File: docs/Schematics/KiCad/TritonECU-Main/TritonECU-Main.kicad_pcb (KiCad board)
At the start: 4 copper layers, 158 x 174 mm, 195 parts, among them J1 EEC-V 104, J301 VR spare, Q101 ISL9V3040S3ST, Q102 ISL9V3040S3ST, Q103 ISL9V3040S3ST, Q104 ISL9V3040S3ST, Q105 ISL9V3040S3ST, Q106 ISL9V3040S3ST, Q107 ISL9V3040S3ST, Q108 ISL9V3040S3ST, Q109 BSS138, Q201 ZXMS6005DGQTA, Q202 ZXMS6005DGQTA, Q203 ZXMS6005DGQTA, Q204 ZXMS6005DGQTA, Q205 ZXMS6005DGQTA, Q206 ZXMS6005DGQTA, Q207 ZXMS6005DGQTA, Q208 ZXMS6005DGQTA, Q401 NCV8405ASTT1G, Q402 NCV8405ASTT1G, Q403 NCV8405ASTT1G, Q404 NCV8405ASTT1G, Q405 NCV8405ASTT1G, Q406 NCV8405ASTT1G, Q407 NCV8405ASTT1G, Q408 NCV8405ASTT1G, Q501 NCV8405ASTT1G, Q502 NCV8405ASTT1G, Q503 NCV8405ASTT1G, Q504 NCV8408BDTRKG, Q505 NCV8405ASTT1G, Q506 NCV8405ASTT1G, Q507 NCV8405ASTT1G, U101 74HCT541, U102 TPS3823A-33DBVR, U301 MAX9926UAEE+T, U302 MAX9926UAEE+T, U303 MAX9926UAEE+T, U401 74HCT541, U402 74HC4051, U501 74HCT541, U601 TBD62083AFNG

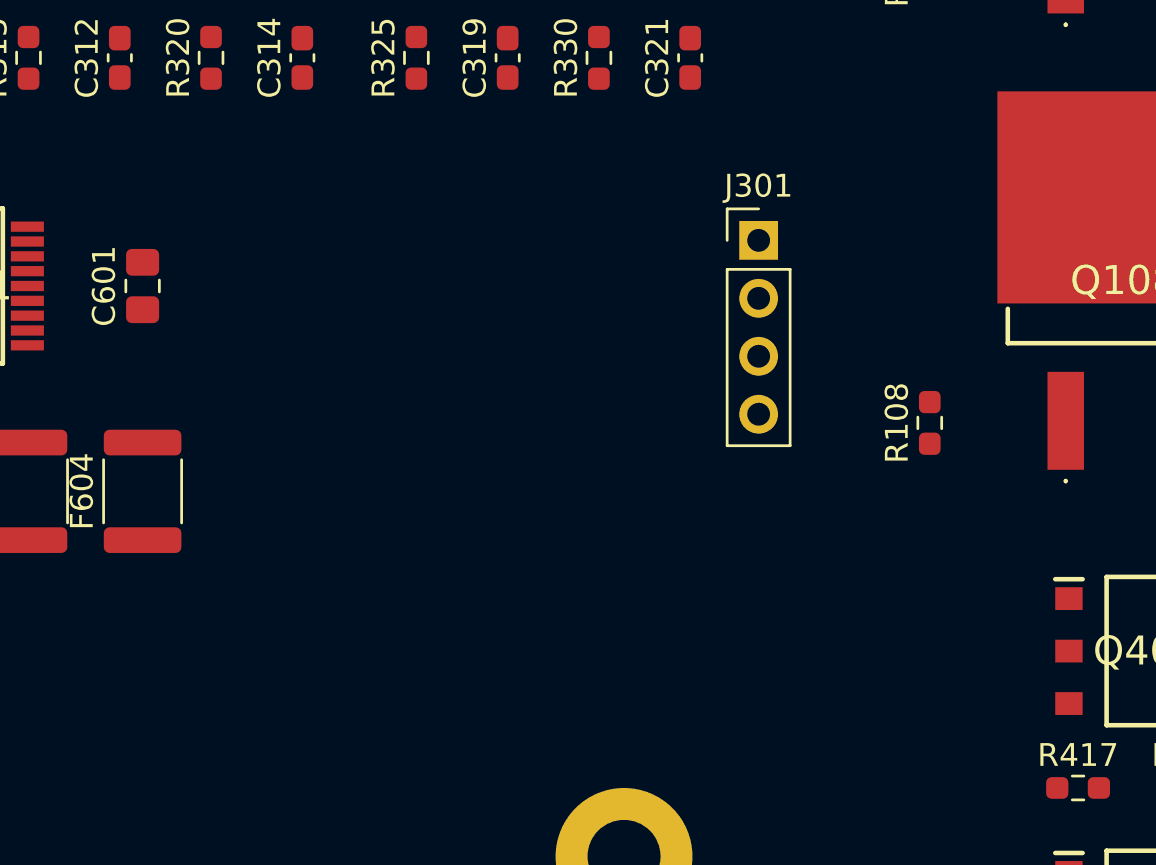
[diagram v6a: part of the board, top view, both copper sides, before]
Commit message: Carrier: VREF sheet, and the power board's +VIN is VPROT, not VPWR
VREF: NCV8772C 5.00 V on the protected rail, EN from the MCU; TPS2H160B-Q1
at 248 mA per feed, latch mode; LM74700-Q1 + DMN6040 ideal diode and
SMAJ24CA per feed; 100k/12.4k short-to-battery sense. Channel 2 drawn,
not fitted (one VREF pin, 90).

Fix: power board J3 +VIN is the LTC4364 OUTPUT (IC1 pin 1, after R2).
The carrier had it on VPWR, joining the surge stopper's output to its
raw input. It is now its own net, VPROT, which also feeds VREF.

gen_carrier_pcb.py: no-connect pins get their unconnected net (parity),
and --replace-sheet NAME re-places one sheet's parts.

Co-Authored-By: Claude Opus 5.5 <noreply@anthropic.com>
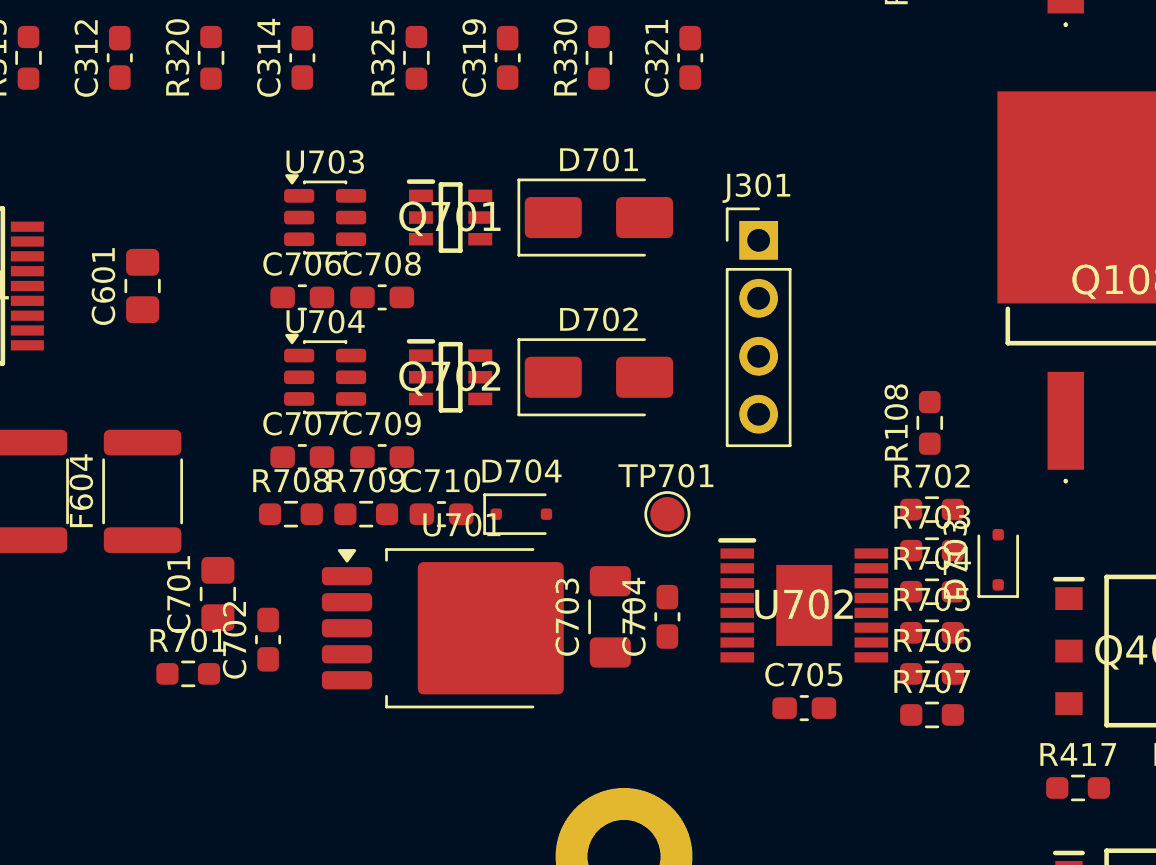
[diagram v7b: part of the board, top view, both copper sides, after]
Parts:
- added C701: 1u, Capacitor_SMD:C_0805_2012Metric_Pad1.18x1.45mm_HandSolder, F.Cu at (136.3, 113.5)
- added C702: 100n, Capacitor_SMD:C_0603_1608Metric_Pad1.08x0.95mm_HandSolder, F.Cu at (138.5, 115.5)
- added C703: 22u, Capacitor_SMD:C_1206_3216Metric_Pad1.33x1.80mm_HandSolder, F.Cu at (153.5, 114.5)
- added C704: 100n, Capacitor_SMD:C_0603_1608Metric_Pad1.08x0.95mm_HandSolder, F.Cu at (156.0, 114.5)
- added C705: 100n, Capacitor_SMD:C_0603_1608Metric_Pad1.08x0.95mm_HandSolder, F.Cu at (162.0, 118.5)
- added C706: 100n, Capacitor_SMD:C_0603_1608Metric_Pad1.08x0.95mm_HandSolder, F.Cu at (140.0, 100.5)
- added C707: 100n, Capacitor_SMD:C_0603_1608Metric_Pad1.08x0.95mm_HandSolder, F.Cu at (140.0, 107.5)
- added C708: 22n, Capacitor_SMD:C_0603_1608Metric_Pad1.08x0.95mm_HandSolder, F.Cu at (143.5, 100.5)
- added C709: 22n, Capacitor_SMD:C_0603_1608Metric_Pad1.08x0.95mm_HandSolder, F.Cu at (143.5, 107.5)
- added C710: 10n, Capacitor_SMD:C_0603_1608Metric_Pad1.08x0.95mm_HandSolder, F.Cu at (146.1, 110.0)
- added D701: SMAJ24CA, Diode_SMD:D_SMA, F.Cu at (153.0, 97.0)
- added D702: SMAJ24CA, Diode_SMD:D_SMA, F.Cu at (153.0, 104.0)
- added D703: BAT54J, Diode_SMD:D_SOD-323F, F.Cu at (170.5, 112.0)
- added D704: BAT54J, Diode_SMD:D_SOD-323F, F.Cu at (149.6, 110.0)
- added Q701: DMN6040SVTQ-7, Samacsys:SOT95P280X100-6N, F.Cu at (146.5, 97.0)
- added Q702: DMN6040SVTQ-7, Samacsys:SOT95P280X100-6N, F.Cu at (146.5, 104.0)
- added R701: 100k, Resistor_SMD:R_0603_1608Metric_Pad0.98x0.95mm_HandSolder, F.Cu at (135.0, 117.0)
- added R702: 10k, Resistor_SMD:R_0603_1608Metric_Pad0.98x0.95mm_HandSolder, F.Cu at (167.6, 109.8)
- added R703: 10k, Resistor_SMD:R_0603_1608Metric_Pad0.98x0.95mm_HandSolder, F.Cu at (167.6, 111.6)
- added R704: 10k, Resistor_SMD:R_0603_1608Metric_Pad0.98x0.95mm_HandSolder, F.Cu at (167.6, 113.4)
- added R705: 2.2k, Resistor_SMD:R_0603_1608Metric_Pad0.98x0.95mm_HandSolder, F.Cu at (167.6, 115.2)
- added R706: 4.7k, Resistor_SMD:R_0603_1608Metric_Pad0.98x0.95mm_HandSolder, F.Cu at (167.6, 117.0)
- added R707: 8.06k, Resistor_SMD:R_0603_1608Metric_Pad0.98x0.95mm_HandSolder, F.Cu at (167.6, 118.8)
- added R708: 100k, Resistor_SMD:R_0603_1608Metric_Pad0.98x0.95mm_HandSolder, F.Cu at (139.5, 110.0)
- added R709: 12.4k, Resistor_SMD:R_0603_1608Metric_Pad0.98x0.95mm_HandSolder, F.Cu at (142.8, 110.0)
- added TP701: VREF2, TestPoint:TestPoint_Pad_D1.5mm, F.Cu at (156.0, 110.0)
- added U701: NCV8772CDT504RKG, Package_TO_SOT_SMD:TO-252-5_TabPin3, F.Cu at (147.0, 115.0)
- added U702: TPS2H160BQPWPRQ1, Samacsys:SOP65P640X120-17N, F.Cu at (162.0, 114.0)
- added U703: LM74700QDBVRQ1, Package_TO_SOT_SMD:SOT-23-6, F.Cu at (141.0, 97.0)
- added U704: LM74700QDBVRQ1, Package_TO_SOT_SMD:SOT-23-6, F.Cu at (141.0, 104.0)
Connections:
- DB1 pad B3: VPWR -> VPROT
- DB1 pad B4: VPWR -> VPROT

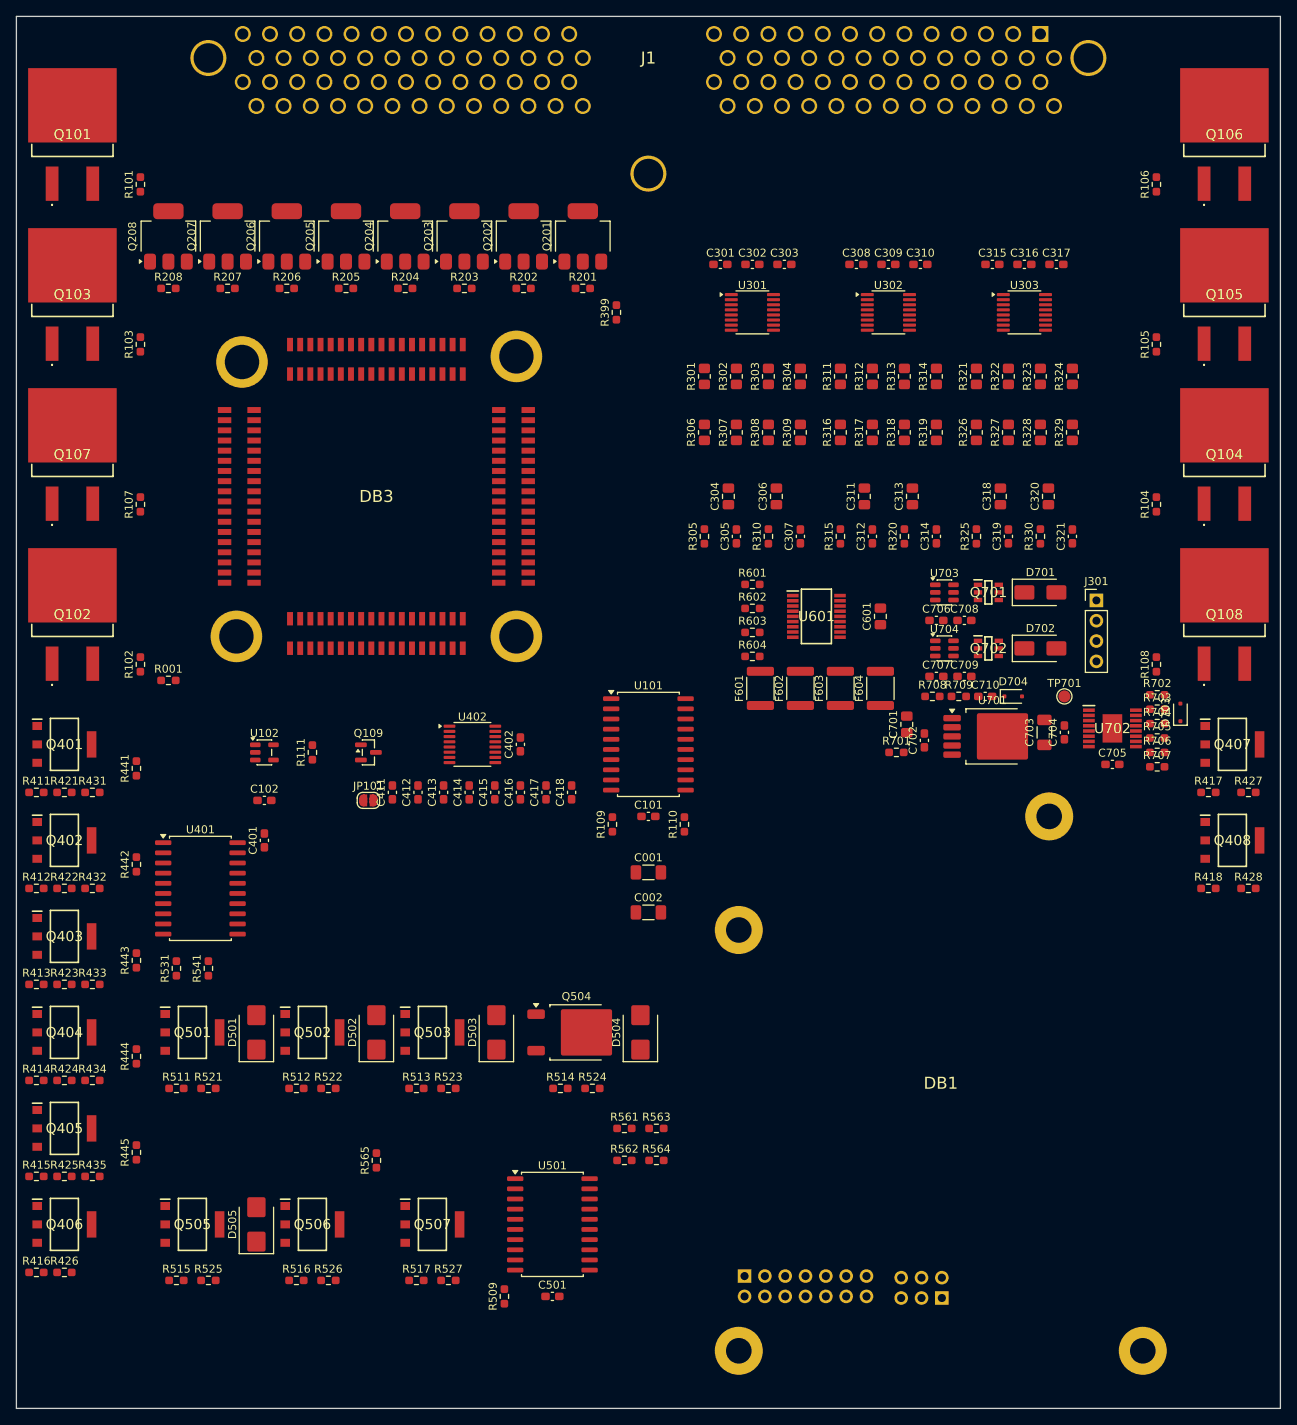
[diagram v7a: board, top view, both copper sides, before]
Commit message: Carrier: ADC sheet (ADS8588H, reference, HO2S buffers, knock, slow channels)
ADS8588H serial on DOUTA, +-10 V, external MAX6070AAUT25 gated by the new
ADC_REF_EN (PG10). MAF differential on ch 1, battery 180k/30k on pin 55,
VREF_5V on ch 8. HO2S x4 per o2-input-stage.md on OPA2376. Knock charge
amp on TLV9064, moved to +3.3 V with a 1.8 V VMID because it lands on a
3.3 V MCU ADC pin. DPFE, TFT, FP monitor conditioned for the MCU ADC.
Series R on the unbuffered channels fitted 0R pending [DECIDE].

gen_carrier_pcb.py: PACK groups placed by courtyard shelf packing.
gen_carrier.py: own dual/quad op-amp symbols, fills an empty placeholder
sheet and keeps its block uuid.

Co-Authored-By: Claude Opus 5.5 <noreply@anthropic.com>
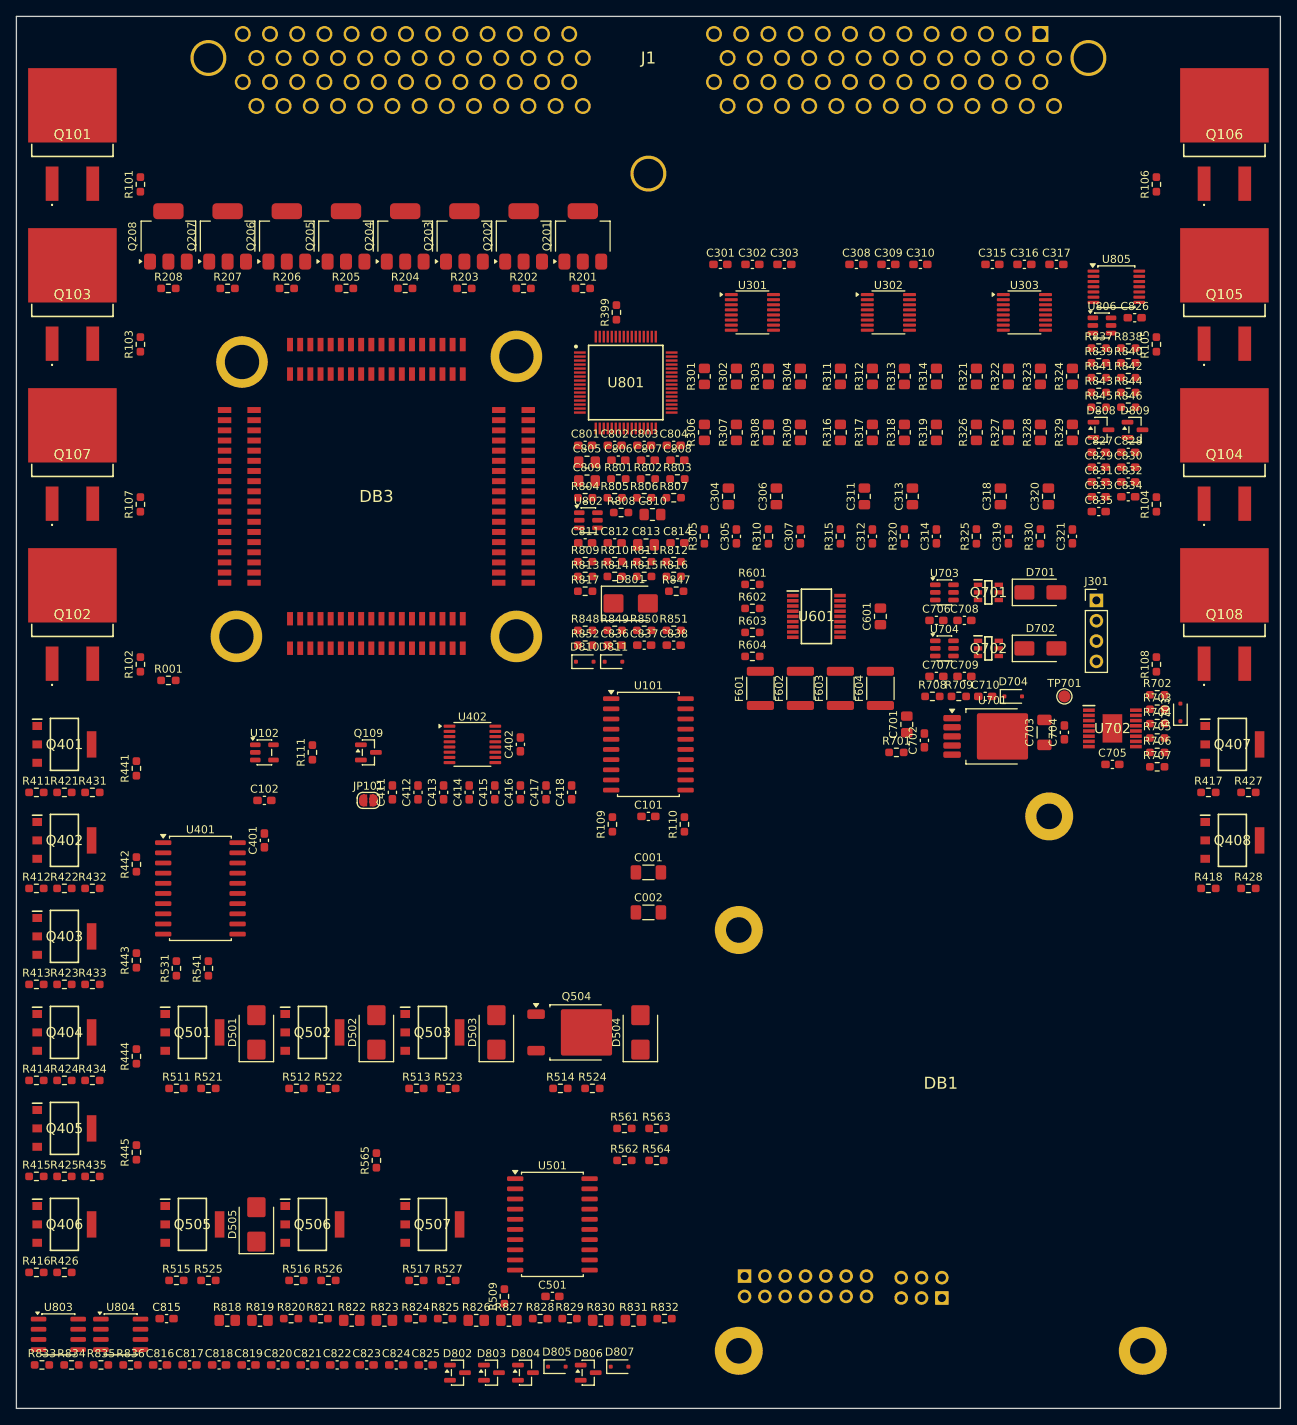
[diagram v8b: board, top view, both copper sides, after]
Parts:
- added C801: 100n, Capacitor_SMD:C_0603_1608Metric_Pad1.08x0.95mm_HandSolder, F.Cu at (96.1, 78.6)
- added C802: 100n, Capacitor_SMD:C_0603_1608Metric_Pad1.08x0.95mm_HandSolder, F.Cu at (99.8, 78.6)
- added C803: 100n, Capacitor_SMD:C_0603_1608Metric_Pad1.08x0.95mm_HandSolder, F.Cu at (103.5, 78.6)
- added C804: 100n, Capacitor_SMD:C_0603_1608Metric_Pad1.08x0.95mm_HandSolder, F.Cu at (107.2, 78.6)
- added C805: 10u, Capacitor_SMD:C_0805_2012Metric_Pad1.18x1.45mm_HandSolder, F.Cu at (96.3, 80.7)
- added C806: 100n, Capacitor_SMD:C_0603_1608Metric_Pad1.08x0.95mm_HandSolder, F.Cu at (100.2, 80.5)
- added C807: 1u, Capacitor_SMD:C_0603_1608Metric_Pad1.08x0.95mm_HandSolder, F.Cu at (103.9, 80.5)
- added C808: 1u, Capacitor_SMD:C_0603_1608Metric_Pad1.08x0.95mm_HandSolder, F.Cu at (107.6, 80.5)
- added C809: 10u, Capacitor_SMD:C_0805_2012Metric_Pad1.18x1.45mm_HandSolder, F.Cu at (96.3, 83.1)
- added C810: 10u, Capacitor_SMD:C_0805_2012Metric_Pad1.18x1.45mm_HandSolder, F.Cu at (104.5, 87.3)
- added C811: 100n, Capacitor_SMD:C_0603_1608Metric_Pad1.08x0.95mm_HandSolder, F.Cu at (96.1, 90.8)
- added C812: 100n, Capacitor_SMD:C_0603_1608Metric_Pad1.08x0.95mm_HandSolder, F.Cu at (99.8, 90.8)
- added C813: 4.7u, Capacitor_SMD:C_0805_2012Metric_Pad1.18x1.45mm_HandSolder, F.Cu at (103.7, 91.1)
- added C814: 100n, Capacitor_SMD:C_0603_1608Metric_Pad1.08x0.95mm_HandSolder, F.Cu at (107.6, 90.8)
- added C815: 100n, Capacitor_SMD:C_0603_1608Metric_Pad1.08x0.95mm_HandSolder, F.Cu at (43.8, 187.8)
- added C816: 1n, Capacitor_SMD:C_0603_1608Metric_Pad1.08x0.95mm_HandSolder, F.Cu at (43.0, 193.6)
- added C817: 1u, Capacitor_SMD:C_0603_1608Metric_Pad1.08x0.95mm_HandSolder, F.Cu at (46.6, 193.6)
- added C818: 1n, Capacitor_SMD:C_0603_1608Metric_Pad1.08x0.95mm_HandSolder, F.Cu at (50.3, 193.6)
- added C819: 1u, Capacitor_SMD:C_0603_1608Metric_Pad1.08x0.95mm_HandSolder, F.Cu at (54.0, 193.6)
- added C820: 100n, Capacitor_SMD:C_0603_1608Metric_Pad1.08x0.95mm_HandSolder, F.Cu at (57.7, 193.6)
- added C821: 1n, Capacitor_SMD:C_0603_1608Metric_Pad1.08x0.95mm_HandSolder, F.Cu at (61.4, 193.6)
- added C822: 1u, Capacitor_SMD:C_0603_1608Metric_Pad1.08x0.95mm_HandSolder, F.Cu at (65.1, 193.6)
- added C823: 1n, Capacitor_SMD:C_0603_1608Metric_Pad1.08x0.95mm_HandSolder, F.Cu at (68.8, 193.6)
- added C824: 1u, Capacitor_SMD:C_0603_1608Metric_Pad1.08x0.95mm_HandSolder, F.Cu at (72.5, 193.6)
- added C825: 100n, Capacitor_SMD:C_0603_1608Metric_Pad1.08x0.95mm_HandSolder, F.Cu at (76.2, 193.6)
- added C826: 100n, Capacitor_SMD:C_0603_1608Metric_Pad1.08x0.95mm_HandSolder, F.Cu at (164.8, 62.7)
- added C827: 220p, Capacitor_SMD:C_0603_1608Metric_Pad1.08x0.95mm_HandSolder, F.Cu at (160.3, 79.5)
- added C828: 220p, Capacitor_SMD:C_0603_1608Metric_Pad1.08x0.95mm_HandSolder, F.Cu at (164.0, 79.5)
- added C829: 620p, Capacitor_SMD:C_0603_1608Metric_Pad1.08x0.95mm_HandSolder, F.Cu at (160.3, 81.3)
- added C830: 620p, Capacitor_SMD:C_0603_1608Metric_Pad1.08x0.95mm_HandSolder, F.Cu at (164.0, 81.3)
- added C831: 15n, Capacitor_SMD:C_0603_1608Metric_Pad1.08x0.95mm_HandSolder, F.Cu at (160.3, 83.2)
- added C832: 100n, Capacitor_SMD:C_0603_1608Metric_Pad1.08x0.95mm_HandSolder, F.Cu at (164.0, 83.2)
- added C833: 100n, Capacitor_SMD:C_0603_1608Metric_Pad1.08x0.95mm_HandSolder, F.Cu at (160.3, 85.0)
- added C834: 1u, Capacitor_SMD:C_0603_1608Metric_Pad1.08x0.95mm_HandSolder, F.Cu at (164.0, 85.0)
- added C835: 1u, Capacitor_SMD:C_0603_1608Metric_Pad1.08x0.95mm_HandSolder, F.Cu at (160.3, 86.9)
- added C836: 10n, Capacitor_SMD:C_0603_1608Metric_Pad1.08x0.95mm_HandSolder, F.Cu at (99.8, 103.6)
- added C837: 100n, Capacitor_SMD:C_0603_1608Metric_Pad1.08x0.95mm_HandSolder, F.Cu at (103.5, 103.6)
- added C838: 100n, Capacitor_SMD:C_0603_1608Metric_Pad1.08x0.95mm_HandSolder, F.Cu at (107.2, 103.6)
- added D801: SMBJ30A, Diode_SMD:D_SMB, F.Cu at (101.8, 98.4)
- added D802: BAT54S, Package_TO_SOT_SMD:SOT-23, F.Cu at (80.1, 194.5)
- added D803: BAT54S, Package_TO_SOT_SMD:SOT-23, F.Cu at (84.4, 194.5)
- added D804: BAT54S, Package_TO_SOT_SMD:SOT-23, F.Cu at (88.6, 194.5)
- added D805: BAT54J, Diode_SMD:D_SOD-323F, F.Cu at (92.6, 193.8)
- added D806: BAT54S, Package_TO_SOT_SMD:SOT-23, F.Cu at (96.5, 194.5)
- added D807: BAT54J, Diode_SMD:D_SOD-323F, F.Cu at (100.4, 193.8)
- added D808: BAV199, Package_TO_SOT_SMD:SOT-23, F.Cu at (160.6, 76.7)
- added D809: BAV199, Package_TO_SOT_SMD:SOT-23, F.Cu at (164.8, 76.7)
- added D810: BAT54J, Diode_SMD:D_SOD-323F, F.Cu at (96.0, 105.7)
- added D811: BAT54J, Diode_SMD:D_SOD-323F, F.Cu at (99.6, 105.7)
- added R801: 0, Resistor_SMD:R_0603_1608Metric_Pad0.98x0.95mm_HandSolder, F.Cu at (100.2, 82.8)
- added R802: 10k, Resistor_SMD:R_0603_1608Metric_Pad0.98x0.95mm_HandSolder, F.Cu at (103.9, 82.8)
- added R803: 10k, Resistor_SMD:R_0603_1608Metric_Pad0.98x0.95mm_HandSolder, F.Cu at (107.6, 82.8)
- added R804: 10k, Resistor_SMD:R_0603_1608Metric_Pad0.98x0.95mm_HandSolder, F.Cu at (96.1, 85.2)
- added R805: 10k, Resistor_SMD:R_0603_1608Metric_Pad0.98x0.95mm_HandSolder, F.Cu at (99.8, 85.2)
- added R806: 10k, Resistor_SMD:R_0603_1608Metric_Pad0.98x0.95mm_HandSolder, F.Cu at (103.5, 85.2)
- added R807: 10k, Resistor_SMD:R_0603_1608Metric_Pad0.98x0.95mm_HandSolder, F.Cu at (107.2, 85.2)
- added R808: 220, Resistor_SMD:R_0603_1608Metric_Pad0.98x0.95mm_HandSolder, F.Cu at (100.6, 87.0)
- added R809: 10k, Resistor_SMD:R_0603_1608Metric_Pad0.98x0.95mm_HandSolder, F.Cu at (96.1, 93.2)
- added R810: 0, Resistor_SMD:R_0603_1608Metric_Pad0.98x0.95mm_HandSolder, F.Cu at (99.8, 93.2)
- added R811: 0, Resistor_SMD:R_0603_1608Metric_Pad0.98x0.95mm_HandSolder, F.Cu at (103.5, 93.2)
- added R812: 0, Resistor_SMD:R_0603_1608Metric_Pad0.98x0.95mm_HandSolder, F.Cu at (107.2, 93.2)
- added R813: 0, Resistor_SMD:R_0603_1608Metric_Pad0.98x0.95mm_HandSolder, F.Cu at (96.1, 95.0)
- added R814: 2.49k, Resistor_SMD:R_0603_1608Metric_Pad0.98x0.95mm_HandSolder, F.Cu at (99.8, 95.0)
- added R815: 2.49k, Resistor_SMD:R_0603_1608Metric_Pad0.98x0.95mm_HandSolder, F.Cu at (103.5, 95.0)
- added R816: 180k, Resistor_SMD:R_0603_1608Metric_Pad0.98x0.95mm_HandSolder, F.Cu at (107.2, 95.0)
- added R817: 30k, Resistor_SMD:R_0603_1608Metric_Pad0.98x0.95mm_HandSolder, F.Cu at (96.1, 96.9)
- added R818: 10k, Resistor_SMD:R_0805_2012Metric_Pad1.20x1.40mm_HandSolder, F.Cu at (51.4, 188.0)
- added R819: 22M, Resistor_SMD:R_0805_2012Metric_Pad1.20x1.40mm_HandSolder, F.Cu at (55.4, 188.0)
- added R820: 1k, Resistor_SMD:R_0603_1608Metric_Pad0.98x0.95mm_HandSolder, F.Cu at (59.3, 187.8)
- added R821: 0, Resistor_SMD:R_0603_1608Metric_Pad0.98x0.95mm_HandSolder, F.Cu at (63.0, 187.8)
- added R822: 10k, Resistor_SMD:R_0805_2012Metric_Pad1.20x1.40mm_HandSolder, F.Cu at (66.9, 188.0)
- added R823: 22M, Resistor_SMD:R_0805_2012Metric_Pad1.20x1.40mm_HandSolder, F.Cu at (71.0, 188.0)
- added R824: 1k, Resistor_SMD:R_0603_1608Metric_Pad0.98x0.95mm_HandSolder, F.Cu at (74.9, 187.8)
- added R825: 0, Resistor_SMD:R_0603_1608Metric_Pad0.98x0.95mm_HandSolder, F.Cu at (78.6, 187.8)
- added R826: 10k, Resistor_SMD:R_0805_2012Metric_Pad1.20x1.40mm_HandSolder, F.Cu at (82.5, 188.0)
- added R827: 22M, Resistor_SMD:R_0805_2012Metric_Pad1.20x1.40mm_HandSolder, F.Cu at (86.6, 188.0)
- added R828: 1k, Resistor_SMD:R_0603_1608Metric_Pad0.98x0.95mm_HandSolder, F.Cu at (90.5, 187.8)
- added R829: 0, Resistor_SMD:R_0603_1608Metric_Pad0.98x0.95mm_HandSolder, F.Cu at (94.1, 187.8)
- added R830: 10k, Resistor_SMD:R_0805_2012Metric_Pad1.20x1.40mm_HandSolder, F.Cu at (98.0, 188.0)
- added R831: 22M, Resistor_SMD:R_0805_2012Metric_Pad1.20x1.40mm_HandSolder, F.Cu at (102.1, 188.0)
- added R832: 1k, Resistor_SMD:R_0603_1608Metric_Pad0.98x0.95mm_HandSolder, F.Cu at (106.0, 187.8)
- added R833: 0, Resistor_SMD:R_0603_1608Metric_Pad0.98x0.95mm_HandSolder, F.Cu at (28.2, 193.6)
- added R834: 91k, Resistor_SMD:R_0603_1608Metric_Pad0.98x0.95mm_HandSolder, F.Cu at (31.9, 193.6)
- added R835: 9.1k, Resistor_SMD:R_0603_1608Metric_Pad0.98x0.95mm_HandSolder, F.Cu at (35.6, 193.6)
- added R836: 1k, Resistor_SMD:R_0603_1608Metric_Pad0.98x0.95mm_HandSolder, F.Cu at (39.3, 193.6)
- added R837: 1k, Resistor_SMD:R_0603_1608Metric_Pad0.98x0.95mm_HandSolder, F.Cu at (160.3, 66.5)
- added R838: 1M, Resistor_SMD:R_0603_1608Metric_Pad0.98x0.95mm_HandSolder, F.Cu at (164.0, 66.5)
- added R839: 1k, Resistor_SMD:R_0603_1608Metric_Pad0.98x0.95mm_HandSolder, F.Cu at (160.3, 68.3)
- added R840: 1M, Resistor_SMD:R_0603_1608Metric_Pad0.98x0.95mm_HandSolder, F.Cu at (164.0, 68.3)
- added R841: 10k, Resistor_SMD:R_0603_1608Metric_Pad0.98x0.95mm_HandSolder, F.Cu at (160.3, 70.2)
- added R842: 10k, Resistor_SMD:R_0603_1608Metric_Pad0.98x0.95mm_HandSolder, F.Cu at (164.0, 70.2)
- added R843: 10k, Resistor_SMD:R_0603_1608Metric_Pad0.98x0.95mm_HandSolder, F.Cu at (160.3, 72.0)
- added R844: 10k, Resistor_SMD:R_0603_1608Metric_Pad0.98x0.95mm_HandSolder, F.Cu at (164.0, 72.0)
- added R845: 470, Resistor_SMD:R_0603_1608Metric_Pad0.98x0.95mm_HandSolder, F.Cu at (160.3, 73.9)
- added R846: 100, Resistor_SMD:R_0603_1608Metric_Pad0.98x0.95mm_HandSolder, F.Cu at (164.0, 73.9)
- added R847: 10k, Resistor_SMD:R_0603_1608Metric_Pad0.98x0.95mm_HandSolder, F.Cu at (107.5, 96.9)
- added R848: 18k, Resistor_SMD:R_0603_1608Metric_Pad0.98x0.95mm_HandSolder, F.Cu at (96.1, 101.7)
- added R849: 2.2k, Resistor_SMD:R_0603_1608Metric_Pad0.98x0.95mm_HandSolder, F.Cu at (99.8, 101.7)
- added R850: 1k, Resistor_SMD:R_0603_1608Metric_Pad0.98x0.95mm_HandSolder, F.Cu at (103.5, 101.7)
- added R851: 100k, Resistor_SMD:R_0603_1608Metric_Pad0.98x0.95mm_HandSolder, F.Cu at (107.2, 101.7)
- added R852: 10.5k, Resistor_SMD:R_0603_1608Metric_Pad0.98x0.95mm_HandSolder, F.Cu at (96.1, 103.6)
- added U801: ADS8588HIPM, Samacsys:QFP50P1200X1200X160-64N, F.Cu at (101.2, 70.8)
- added U802: MAX6070AAUT25+T, Package_TO_SOT_SMD:SOT-23-6, F.Cu at (96.5, 88.0)
- added U803: OPA2376AQDRQ1, Package_SO:SOIC-8_3.9x4.9mm_P1.27mm, F.Cu at (30.2, 189.7)
- added U804: OPA2376AQDRQ1, Package_SO:SOIC-8_3.9x4.9mm_P1.27mm, F.Cu at (38.0, 189.7)
- added U805: TLV9064QPWRQ1, Package_SO:TSSOP-14_4.4x5mm_P0.65mm, F.Cu at (162.5, 58.8)
- added U806: MAX6070AAUT18+T, Package_TO_SOT_SMD:SOT-23-6, F.Cu at (160.7, 63.6)
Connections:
- DB3 pad D18: unconnected-(DB3-PG10-PadD18) -> ADC_REF_EN
